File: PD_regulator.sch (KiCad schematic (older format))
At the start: 26 parts, among them J5 Switch, J6 Fast_Out, U5 ADA4896-2ARMZ, U8 ADG1413, U9 LTC6228xS8

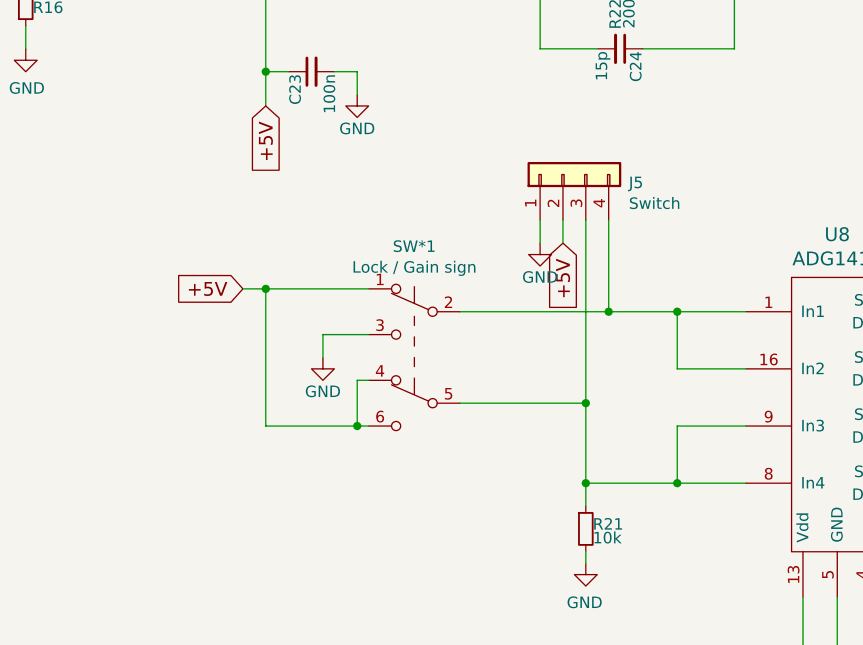
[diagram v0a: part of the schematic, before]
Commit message: Fast PD second draft
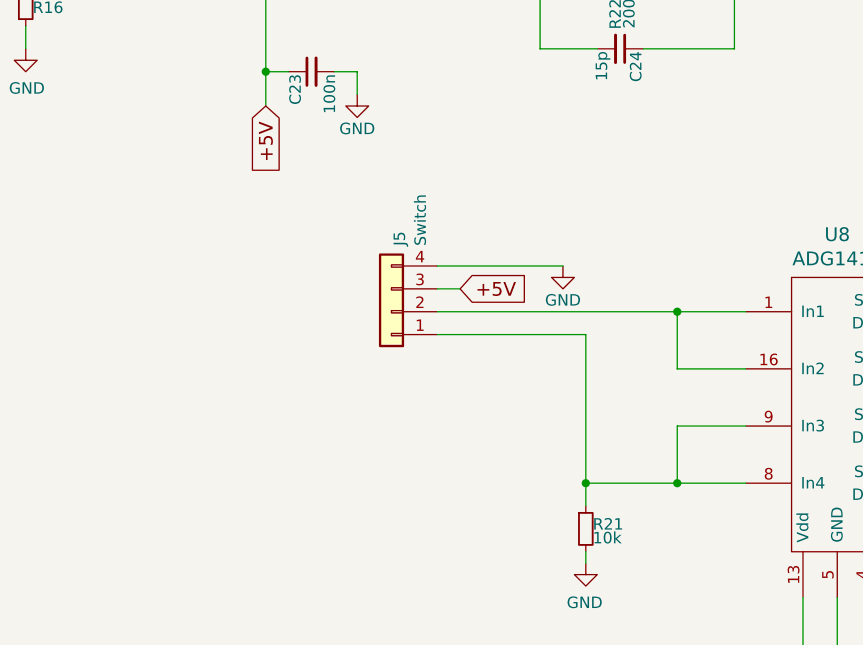
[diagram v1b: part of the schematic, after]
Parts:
- removed SW*1: Lock / Gain sign, symbol Switch:SW_Push_DPDT
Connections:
- net +5V: now also J5.3 (Pin_3); no longer J5.2 (Pin_2)
- net GND: now also J5.4 (Pin_4); no longer J5.1 (Pin_1)
- net at U8.1 (In1), U8.16 (In2): now also J5.2 (Pin_2); no longer J5.4 (Pin_4)
- net at R21.1, U8.8 (In4), U8.9 (In3): now also J5.1 (Pin_1); no longer J5.3 (Pin_3)
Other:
- moved on the sheet: J5
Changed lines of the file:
@@
 Wire Wire Line
 	8800 2400 8700 2400
-Text GLabel 3600 4150 3    60   Input ~ 0
+Text GLabel 3150 4350 2    60   Input ~ 0
 +5V
-$Comp
-L power:GND #PWR0120
-U 1 1 61F6D5A6
-P 2550 4650
-F 0 "#PWR0120" H 2550 4400 50  0001 C CNN
-F 1 "GND" H 2550 4500 50  0000 C CNN
-F 2 "" H 2550 4650 50  0001 C CNN
-F 3 "" H 2550 4650 50  0001 C CNN
-	1    2550 4650
-	1    0    0    -1
-$EndComp
-Wire Wire Line
-	2550 4550 2550 4650
-Wire Wire Line
-	2550 4550 2750 4550
 $Comp
 L Device:R_Small R21
@@
 Text GLabel 5600 5250 2    60   Input ~ 0
 D4
-$Comp
-L Switch:SW_Push_DPDT SW*1
-U 1 1 61F56921
-P 2950 4650
-F 0 "SW*1" H 2950 5135 50  0000 C CNN
-F 1 "Lock / Gain sign" H 2950 5044 50  0000 C CNN
-F 2 "" H 2950 4850 50  0001 C CNN
-F 3 "~" H 2950 4850 50  0001 C CNN
-	1    2950 4650
-	-1   0    0    -1
-$EndComp
 Wire Wire Line
 	4400 4700 4100 4700
@@
 Wire Wire Line
 	4100 4450 4400 4450
-Wire Wire Line
-	4100 4450 3800 4450
 Connection ~ 4100 4450
 Wire Wire Line
-	2750 4950 2700 4950
-Wire Wire Line
-	2300 4950 2300 4350
-Wire Wire Line
-	2300 4350 2750 4350
-Wire Wire Line
-	2750 4750 2700 4750
-Wire Wire Line
-	2700 4750 2700 4950
-Connection ~ 2700 4950
-Wire Wire Line
-	2700 4950 2300 4950
-Wire Wire Line
 	3700 5200 3700 5300
-Wire Wire Line
-	3700 4850 3700 5200
-Wire Wire Line
-	3150 4850 3700 4850
 Connection ~ 3700 5200
-Wire Wire Line
-	2300 4350 2200 4350
-Connection ~ 2300 4350
 Wire Wire Line
 	5200 5250 5500 5250
@@
 L Connector_Generic:Conn_01x04 J5
 U 1 1 620A028C
-P 3600 3850
-F 0 "J5" V 3564 3562 50  0000 R CNN
-F 1 "Switch" V 3473 3562 50  0000 R CNN
-F 2 "Connector_PinHeader_2.54mm:PinHeader_1x04_P2.54mm_Vertical" H 3600 3850 50  0001 C CNN
-F 3 "~" H 3600 3850 50  0001 C CNN
-	1    3600 3850
-	0    -1   -1   0
-$EndComp
-Wire Wire Line
-	3700 4850 3700 4050
-Connection ~ 3700 4850
-Wire Wire Line
-	3800 4450 3800 4050
-Connection ~ 3800 4450
-Wire Wire Line
-	3800 4450 3150 4450
+P 2850 4450
+F 0 "J5" V 2814 4162 50  0000 R CNN
+F 1 "Switch" V 2723 4162 50  0000 R CNN
+F 2 "Connector_PinHeader_2.54mm:PinHeader_1x04_P2.54mm_Vertical" H 2850 4450 50  0001 C CNN
+F 3 "~" H 2850 4450 50  0001 C CNN
+	1    2850 4450
+	-1   0    0    1
+$EndComp
 $Comp
 L power:GND #PWR0125
 U 1 1 620B089E
-P 3500 4150
-F 0 "#PWR0125" H 3500 3900 50  0001 C CNN
-F 1 "GND" H 3500 4000 50  0000 C CNN
-F 2 "" H 3500 4150 50  0001 C CNN
-F 3 "" H 3500 4150 50  0001 C CNN
-	1    3500 4150
-	1    0    0    -1
-$EndComp
-Wire Wire Line
-	3600 4150 3600 4050
-Wire Wire Line
-	3500 4150 3500 4050
-Text GLabel 2200 4350 0    60   Input ~ 0
-+5V
+P 3600 4250
+F 0 "#PWR0125" H 3600 4000 50  0001 C CNN
+F 1 "GND" H 3600 4100 50  0000 C CNN
+F 2 "" H 3600 4250 50  0001 C CNN
+F 3 "" H 3600 4250 50  0001 C CNN
+	1    3600 4250
+	1    0    0    -1
+$EndComp
 Wire Wire Line
 	4400 4950 4100 4950
@@
 Wire Wire Line
 	5700 4900 5700 4950
+Wire Wire Line
+	3050 4550 3700 4550
+Wire Wire Line
+	3700 4550 3700 5200
+Wire Wire Line
+	3050 4450 4100 4450
+Wire Wire Line
+	3600 4250 3050 4250
+Wire Wire Line
+	3150 4350 3050 4350
 $EndSCHEMATC

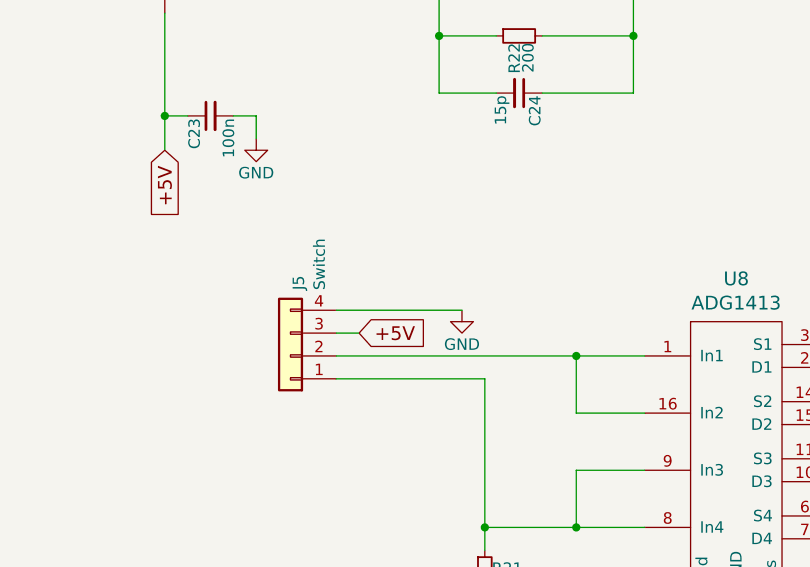
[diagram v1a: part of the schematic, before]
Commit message: Add fast PD regulator
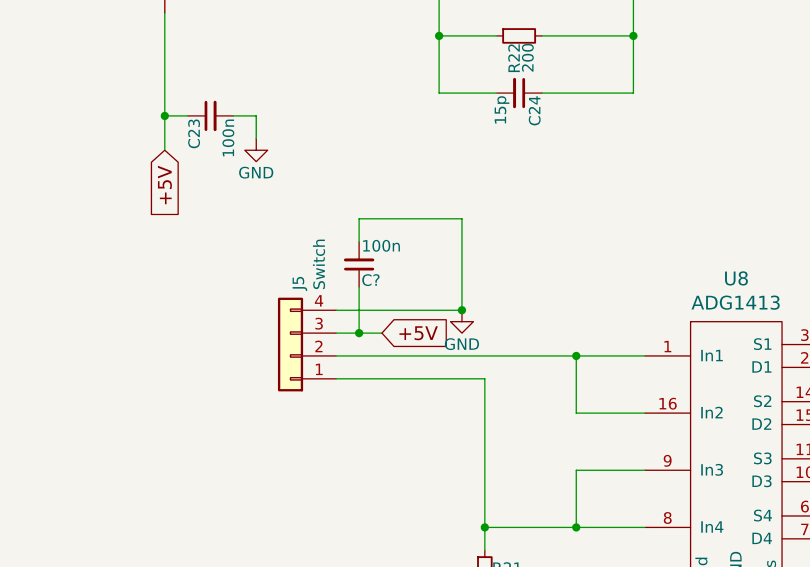
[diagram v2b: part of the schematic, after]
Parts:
- added C?: 100n, Capacitor_SMD:C_0603_1608Metric, symbol Device:C_Small
- J5: footprint Connector_PinHeader_2.54mm:PinHeader_1x04_P2.54mm_Vertical -> Connector_JST:JST_PH_B4B-PH-K_1x04_P2.00mm_Vertical
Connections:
- net +5V: now also C?.1
- net GND: now also C?.2
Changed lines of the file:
@@
 Wire Wire Line
 	8800 2400 8700 2400
-Text GLabel 3150 4350 2    60   Input ~ 0
+Text GLabel 3250 4350 2    60   Input ~ 0
 +5V
 $Comp
@@
 F 0 "J5" V 2814 4162 50  0000 R CNN
 F 1 "Switch" V 2723 4162 50  0000 R CNN
-F 2 "Connector_PinHeader_2.54mm:PinHeader_1x04_P2.54mm_Vertical" H 2850 4450 50  0001 C CNN
+F 2 "Connector_JST:JST_PH_B4B-PH-K_1x04_P2.00mm_Vertical" H 2850 4450 50  0001 C CNN
 F 3 "~" H 2850 4450 50  0001 C CNN
 	1    2850 4450
@@
 Wire Wire Line
 	3150 4350 3050 4350
+$Comp
+L Device:C_Small C?
+U 1 1 61E8ECDD
+P 3150 4050
+F 0 "C?" H 3160 4120 50  0000 L CNN
+F 1 "100n" H 3160 3970 50  0000 L CNN
+F 2 "Capacitor_SMD:C_0603_1608Metric" H 3150 4050 50  0001 C CNN
+F 3 "" H 3150 4050 50  0001 C CNN
+	1    3150 4050
+	1    0    0    1
+$EndComp
+Wire Wire Line
+	3150 4150 3150 4350
+Wire Wire Line
+	3150 4350 3250 4350
+Connection ~ 3150 4350
+Wire Wire Line
+	3150 3950 3150 3850
+Wire Wire Line
+	3150 3850 3600 3850
+Wire Wire Line
+	3600 3850 3600 4250
+Connection ~ 3600 4250
 $EndSCHEMATC

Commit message: Add drawing and comment for switch connection
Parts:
- gave numbers to parts that had none: 1
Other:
- note added: "Use a SPDT toggle switch. Connect \nthe switch as depicted below.\nUp/Down position will change \nthe gain sign. Middle position \nwill disconnect the fast out."
